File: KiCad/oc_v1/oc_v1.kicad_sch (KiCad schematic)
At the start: 22 parts, among them J1 ESC_CTRL, J10 STPR_CTRL, J11 ENC_A, J12 ENC_A, J13 MOTOR, J14 Screw_Terminal_01x02, J2 ESC_SEN, J3 BLDC_SEN, J4 ESC_CTRL, J5 ESC_SEN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

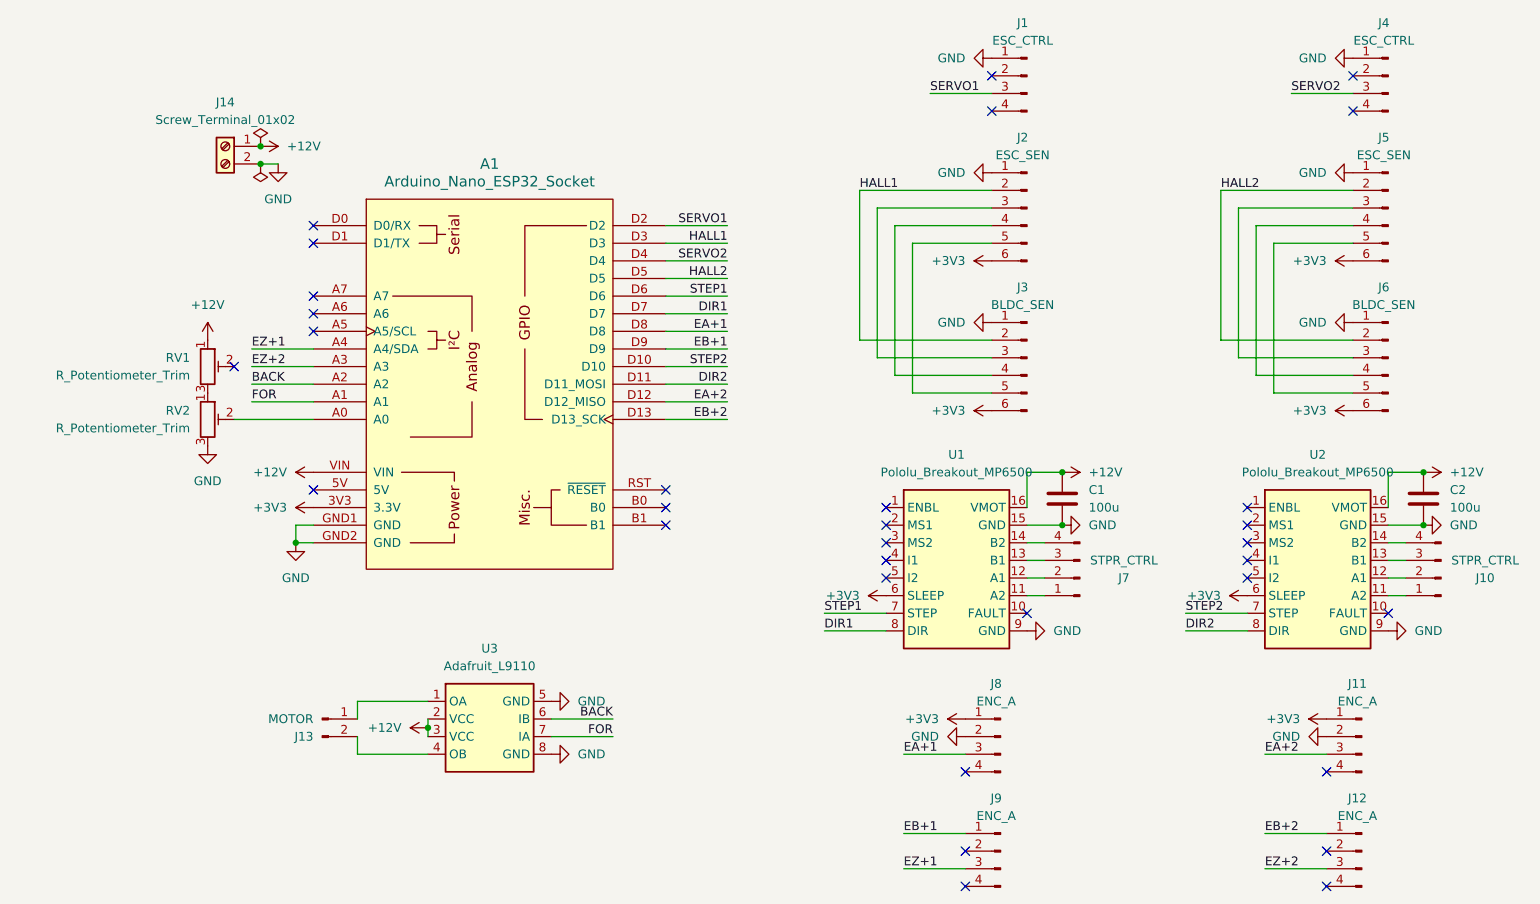
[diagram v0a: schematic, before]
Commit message: Completed onboard controller PCB
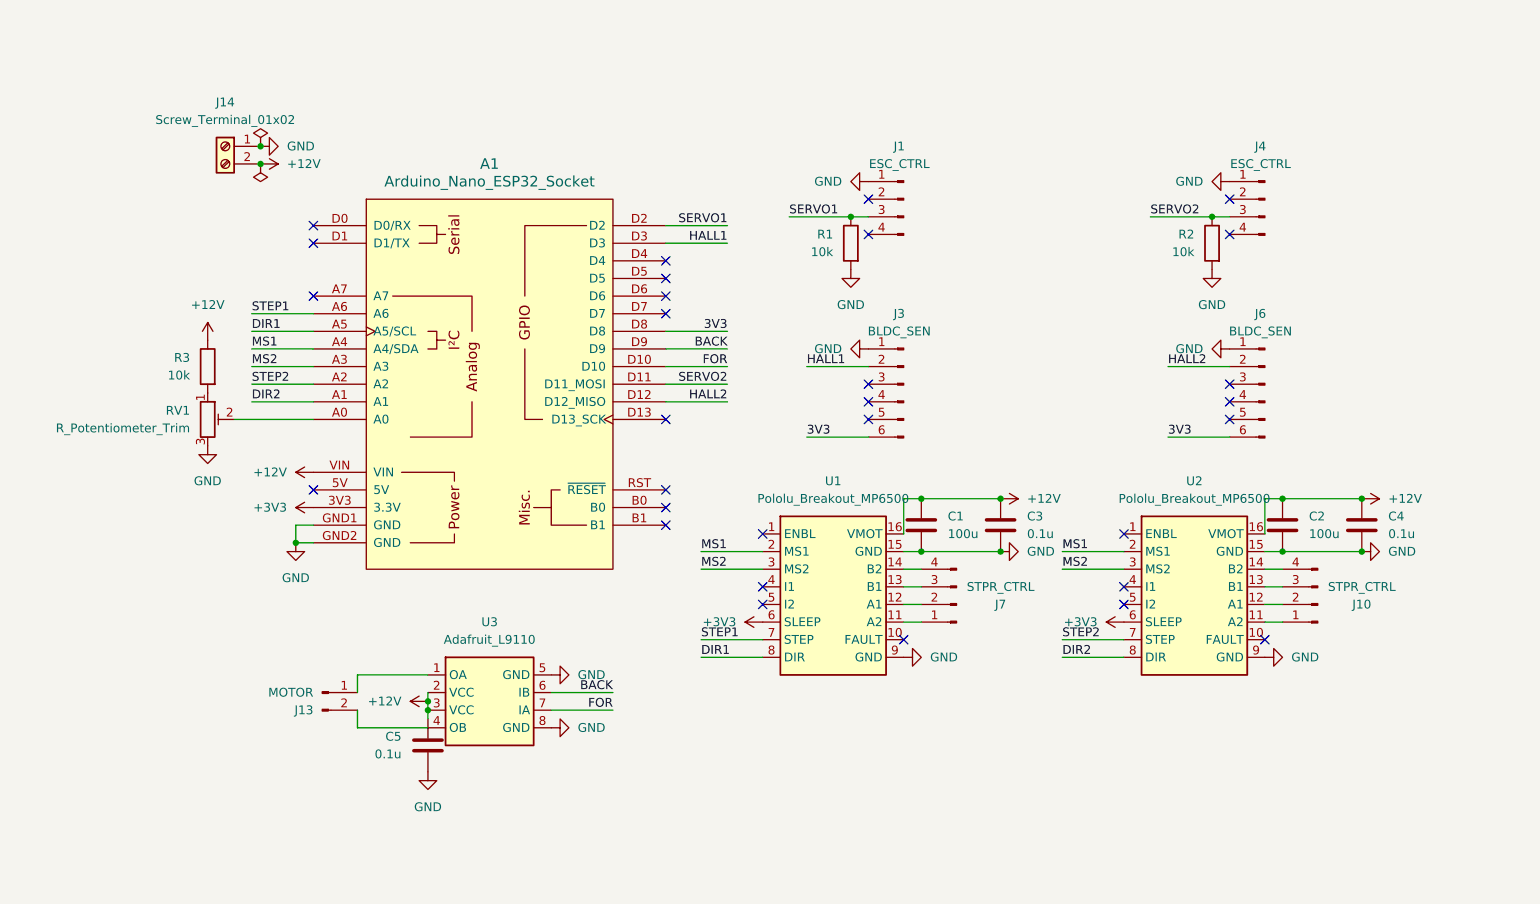
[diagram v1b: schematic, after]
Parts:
- removed J11, J12, J8, J9: ENC_A, Connector_JST:JST_XH_S4B-XH-A_1x04_P2.50mm_Horizontal, symbol Connector:Conn_01x04_Pin
- removed J2, J5: ESC_SEN, Connector_JST:JST_XH_S6B-XH-A_1x06_P2.50mm_Horizontal, symbol Connector:Conn_01x06_Pin
- removed RV2: R_Potentiometer_Trim, Footprint Library:Bourns_TC33X_Potentiometer, symbol Device:R_Potentiometer_Trim
- added C3, C4, C5: 0.1u, Capacitor_SMD:C_0603_1608Metric_Pad1.08x0.95mm_HandSolder, symbol Device:C
- added R1, R2, R3: 10k, Resistor_SMD:R_0805_2012Metric_Pad1.20x1.40mm_HandSolder, symbol Device:R
- C1, C2: footprint (none) -> Capacitor_SMD:C_1210_3225Metric_Pad1.33x2.70mm_HandSolder
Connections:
- net EA+2 is gone; now on net HALL2: A1.D12 (D12_MISO)
- net EB+1 is gone; now on net BACK: A1.D9
- net EZ+1 is gone; now on net MS1: A1.A4 (A4/SDA)
- net EZ+2 is gone; now on net MS2: A1.A3
- net +12V: now also J14.2 (Pin_2), C3.1, C4.1, C5.1, R3.1; no longer J14.1 (Pin_1), RV1.1
- net +3V3: no longer J3.6 (Pin_6), J6.6 (Pin_6)
- net BACK: no longer A1.A2
- net DIR1: now also A1.A5 (A5/SCL); no longer A1.D7
- net DIR2: now also A1.A1; no longer A1.D11 (D11_MOSI)
- net FOR: now also A1.D10; no longer A1.A1
- net GND: now also J14.1 (Pin_1), RV1.3, C3.2, C4.2, C5.2, R1.2, R2.2; no longer J14.2 (Pin_2)
- net HALL2: no longer A1.D5
- net SERVO1: now also R1.1
- net SERVO2: now also A1.D11 (D11_MOSI), R2.1; no longer A1.D4
- net STEP1: now also A1.A6; no longer A1.D6
- net STEP2: now also A1.A2; no longer A1.D10
- net at A1.A0: now also RV1.2
- net MS1: now reaches U1.2 (MS1)
- net MS1: now also U2.2 (MS1)
- net MS2: now reaches U1.3 (MS2)
- net MS2: now also U2.3 (MS2)
- net EA+1 renamed 3V3
- net 3V3: now also J3.6 (Pin_6), J6.6 (Pin_6)
- net EB+2: no longer names the net of A1.D13 (D13_SCK)
- new net: R3.2, RV1.1
- no-connect marks 32 -> 30
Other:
- moved on the sheet: C1, J1, J10, J13, J3, J4, J6, J7, U1, U2, U3

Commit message: fixed problem with pcb
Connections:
- net 3V3 is gone; now on net +3V3: A1.D8, J3.6 (Pin_6), J6.6 (Pin_6)
- net +12V: now also J14.1 (Pin_1); no longer J14.2 (Pin_2)
- net GND: now also J14.2 (Pin_2); no longer J14.1 (Pin_1)
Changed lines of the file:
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@@
   (junction (at 153.67 57.15) (diameter 0) (color 0 0 0 0)
   )
+  (junction (at 68.58 46.99) (diameter 0) (color 0 0 0 0)
+  )
   (junction (at 215.9 105.41) (diameter 0) (color 0 0 0 0)
   )
@@
   (junction (at 175.26 105.41) (diameter 0) (color 0 0 0 0)
   )
+  (junction (at 227.33 97.79) (diameter 0) (color 0 0 0 0)
+  )
   (junction (at 68.58 49.53) (diameter 0) (color 0 0 0 0)
-  )
-  (junction (at 227.33 97.79) (diameter 0) (color 0 0 0 0)
-  )
-  (junction (at 68.58 46.99) (diameter 0) (color 0 0 0 0)
   )
   (junction (at 205.74 57.15) (diameter 0) (color 0 0 0 0)
@@
     (stroke (width 0) (type default))
   )
-  (wire (pts (xy 199.39 88.9) (xy 208.28 88.9))
-    (stroke (width 0) (type default))
-  )
   (wire (pts (xy 215.9 105.41) (xy 227.33 105.41))
     (stroke (width 0) (type default))
@@
     (stroke (width 0) (type default))
   )
-  (wire (pts (xy 147.32 88.9) (xy 156.21 88.9))
-    (stroke (width 0) (type default))
-  )
   (wire (pts (xy 135.89 81.28) (xy 127 81.28))
     (stroke (width 0) (type default))
@@
   )
   (wire (pts (xy 127 58.42) (xy 135.89 58.42))
-    (stroke (width 0) (type default))
-  )
-  (wire (pts (xy 135.89 73.66) (xy 127 73.66))
     (stroke (width 0) (type default))
   )
@@
     (effects (font (size 1.27 1.27)) (justify left bottom))
   )
-  (label "3V3" (at 135.89 73.66 180) (fields_autoplaced)
-    (effects (font (size 1.27 1.27)) (justify right bottom))
-  )
-  (label "3V3" (at 199.39 88.9 0) (fields_autoplaced)
-    (effects (font (size 1.27 1.27)) (justify left bottom))
-  )
   (label "SERVO2" (at 135.89 81.28 180) (fields_autoplaced)
     (effects (font (size 1.27 1.27)) (justify right bottom))
   )
-  (label "3V3" (at 147.32 88.9 0) (fields_autoplaced)
-    (effects (font (size 1.27 1.27)) (justify left bottom))
-  )
   (label "FOR" (at 119.38 128.27 180) (fields_autoplaced)
     (effects (font (size 1.27 1.27)) (justify right bottom))
@@
     (effects (font (size 1.27 1.27)) (justify right bottom))
   )
+  (symbol (lib_id "power:+3V3") (at 127 73.66 270) (unit 1)
+    (in_bom yes) (on_board yes) (dnp no)
+    (property "Reference" "#PWR013" (at 123.19 73.66 0)
+      (effects (font (size 1.27 1.27)) hide)
+    )
+    (property "Value" "+3V3" (at 130.81 73.66 90)
+      (effects (font (size 1.27 1.27)) (justify left))
+    )
+    (property "Footprint" "" (at 127 73.66 0)
+      (effects (font (size 1.27 1.27)) hide)
+    )
+    (property "Datasheet" "" (at 127 73.66 0)
+      (effects (font (size 1.27 1.27)) hide)
+    )
+    (pin "1")
+    (instances
+      (project "oc_v1"
+        (path "/48959e94-00ea-498b-bda9-aa4fe0f03d2c"
+          (reference "#PWR013") (unit 1)
+        )
+      )
+    )
+  )
   (symbol (lib_id "power:+12V") (at 92.71 127 90) (unit 1)
     (in_bom yes) (on_board yes) (dnp no) (fields_autoplaced)
@@
     )
   )
+  (symbol (lib_id "power:GND") (at 68.58 49.53 90) (unit 1)
+    (in_bom yes) (on_board yes) (dnp no) (fields_autoplaced)
+    (property "Reference" "#PWR06" (at 74.93 49.53 0)
+      (effects (font (size 1.27 1.27)) hide)
+    )
+    (property "Value" "GND" (at 72.39 49.53 90)
+      (effects (font (size 1.27 1.27)) (justify right))
+    )
+    (property "Footprint" "" (at 68.58 49.53 0)
+      (effects (font (size 1.27 1.27)) hide)
+    )
+    (property "Datasheet" "" (at 68.58 49.53 0)
+      (effects (font (size 1.27 1.27)) hide)
+    )
+    (pin "1")
+    (instances
+      (project "oc_v1"
+        (path "/48959e94-00ea-498b-bda9-aa4fe0f03d2c"
+          (reference "#PWR06") (unit 1)
+        )
+      )
+    )
+  )
   (symbol (lib_id "Connector:Conn_01x04_Pin") (at 168.91 113.03 180) (unit 1)
     (in_bom yes) (on_board yes) (dnp no)
@@
     )
   )
-  (symbol (lib_id "power:GND") (at 68.58 46.99 90) (unit 1)
-    (in_bom yes) (on_board yes) (dnp no) (fields_autoplaced)
-    (property "Reference" "#PWR06" (at 74.93 46.99 0)
-      (effects (font (size 1.27 1.27)) hide)
-    )
-    (property "Value" "GND" (at 72.39 46.99 90)
-      (effects (font (size 1.27 1.27)) (justify right))
-    )
-    (property "Footprint" "" (at 68.58 46.99 0)
-      (effects (font (size 1.27 1.27)) hide)
-    )
-    (property "Datasheet" "" (at 68.58 46.99 0)
-      (effects (font (size 1.27 1.27)) hide)
-    )
-    (pin "1")
-    (instances
-      (project "oc_v1"
-        (path "/48959e94-00ea-498b-bda9-aa4fe0f03d2c"
-          (reference "#PWR06") (unit 1)
-        )
-      )
-    )
-  )
   (symbol (lib_id "power:GND") (at 110.49 130.81 90) (unit 1)
     (in_bom yes) (on_board yes) (dnp no) (fields_autoplaced)
@@
         (path "/48959e94-00ea-498b-bda9-aa4fe0f03d2c"
           (reference "#PWR03") (unit 1)
+        )
+      )
+    )
+  )
+  (symbol (lib_id "power:+3V3") (at 156.21 88.9 90) (unit 1)
+    (in_bom yes) (on_board yes) (dnp no)
+    (property "Reference" "#PWR014" (at 160.02 88.9 0)
+      (effects (font (size 1.27 1.27)) hide)
+    )
+    (property "Value" "+3V3" (at 152.4 88.9 90)
+      (effects (font (size 1.27 1.27)) (justify left))
+    )
+    (property "Footprint" "" (at 156.21 88.9 0)
+      (effects (font (size 1.27 1.27)) hide)
+    )
+    (property "Datasheet" "" (at 156.21 88.9 0)
+      (effects (font (size 1.27 1.27)) hide)
+    )
+    (pin "1")
+    (instances
+      (project "oc_v1"
+        (path "/48959e94-00ea-498b-bda9-aa4fe0f03d2c"
+          (reference "#PWR014") (unit 1)
         )
       )
@@
     )
   )
-  (symbol (lib_id "power:+12V") (at 68.58 49.53 270) (unit 1)
-    (in_bom yes) (on_board yes) (dnp no)
-    (property "Reference" "#PWR04" (at 64.77 49.53 0)
-      (effects (font (size 1.27 1.27)) hide)
-    )
-    (property "Value" "+12V" (at 72.39 49.53 90)
-      (effects (font (size 1.27 1.27)) (justify left))
-    )
-    (property "Footprint" "" (at 68.58 49.53 0)
-      (effects (font (size 1.27 1.27)) hide)
-    )
-    (property "Datasheet" "" (at 68.58 49.53 0)
+  (symbol (lib_id "power:+12V") (at 68.58 46.99 270) (unit 1)
+    (in_bom yes) (on_board yes) (dnp no)
+    (property "Reference" "#PWR04" (at 64.77 46.99 0)
+      (effects (font (size 1.27 1.27)) hide)
+    )
+    (property "Value" "+12V" (at 72.39 46.99 90)
+      (effects (font (size 1.27 1.27)) (justify left))
+    )
+    (property "Footprint" "" (at 68.58 46.99 0)
+      (effects (font (size 1.27 1.27)) hide)
+    )
+    (property "Datasheet" "" (at 68.58 46.99 0)
       (effects (font (size 1.27 1.27)) hide)
     )
@@
         )
       )
+    )
+  )
+  (symbol (lib_id "power:+3V3") (at 208.28 88.9 90) (unit 1)
+    (in_bom yes) (on_board yes) (dnp no)
+    (property "Reference" "#PWR016" (at 212.09 88.9 0)
+      (effects (font (size 1.27 1.27)) hide)
+    )
+    (property "Value" "+3V3" (at 204.47 88.9 90)
+      (effects (font (size 1.27 1.27)) (justify left))
+    )
+    (property "Footprint" "" (at 208.28 88.9 0)
+      (effects (font (size 1.27 1.27)) hide)
+    )
+    (property "Datasheet" "" (at 208.28 88.9 0)
+      (effects (font (size 1.27 1.27)) hide)
+    )
+    (pin "1")
+    (instances
+      (project "oc_v1"
+        (path "/48959e94-00ea-498b-bda9-aa4fe0f03d2c"
+          (reference "#PWR016") (unit 1)
+        )
+      )

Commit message: revised onboard pcb
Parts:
- removed C1: 100u, Capacitor_SMD:C_1210_3225Metric_Pad1.33x2.70mm_HandSolder, symbol Device:C
- removed C5: 0.1u, Capacitor_SMD:C_0603_1608Metric_Pad1.08x0.95mm_HandSolder, symbol Device:C
- added C1: 100u, Capacitor_THT:CP_Radial_D5.0mm_P2.50mm, symbol Device:C_Polarized
- added D1, D2, D3, D4: D_Zener, Diode_SMD:D_TUMD2, symbol Device:D_Zener
- C2: value 100u -> 0.1u; footprint Capacitor_SMD:C_1210_3225Metric_Pad1.33x2.70mm_HandSolder -> Capacitor_SMD:C_0603_1608Metric_Pad1.08x0.95mm_HandSolder
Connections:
- net +12V: now also C1.1, D1.1 (K), D2.1 (K), D3.1 (K), D4.1 (K)
- net GND: now also C1.2, D1.2 (A), D2.2 (A), D3.2 (A), D4.2 (A)
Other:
- moved on the sheet: J10, J14, J4, J6, R2, R3, RV1, U2
